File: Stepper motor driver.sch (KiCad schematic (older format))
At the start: 16 parts, among them P1 CONN_01X04, P2 CONN_01X04, Q1 TIP120, Q2 TIP120, Q3 TIP120, Q4 TIP120, U1 74LS175, U2 74LS157

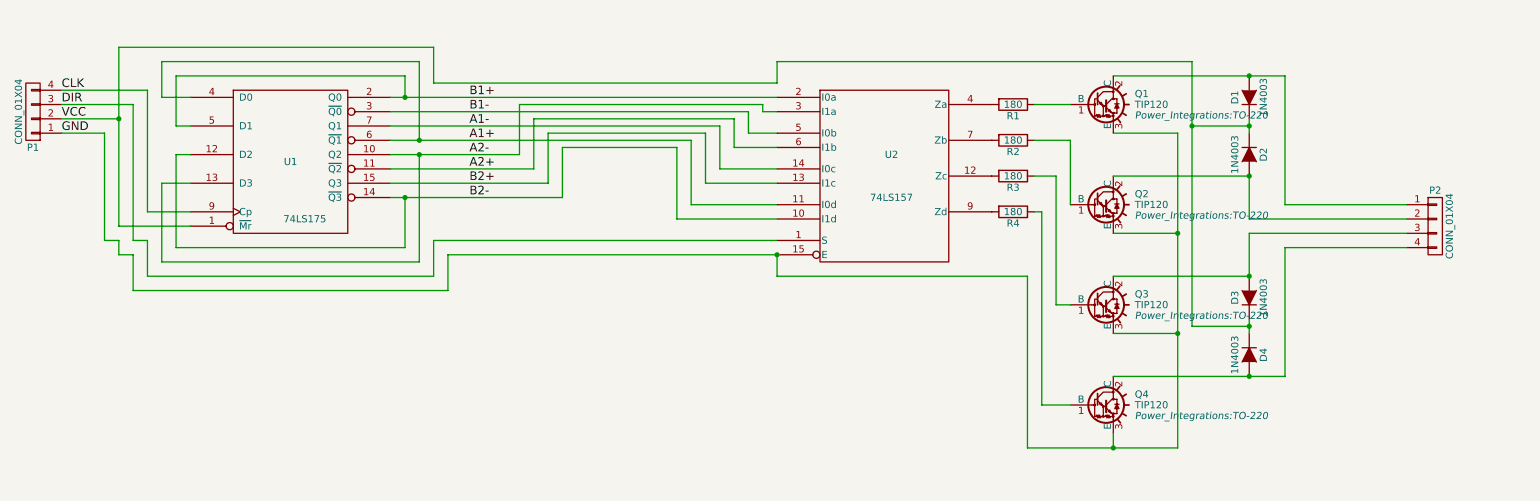
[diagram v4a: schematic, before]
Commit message: Cleaned up schematic and placed PCB components
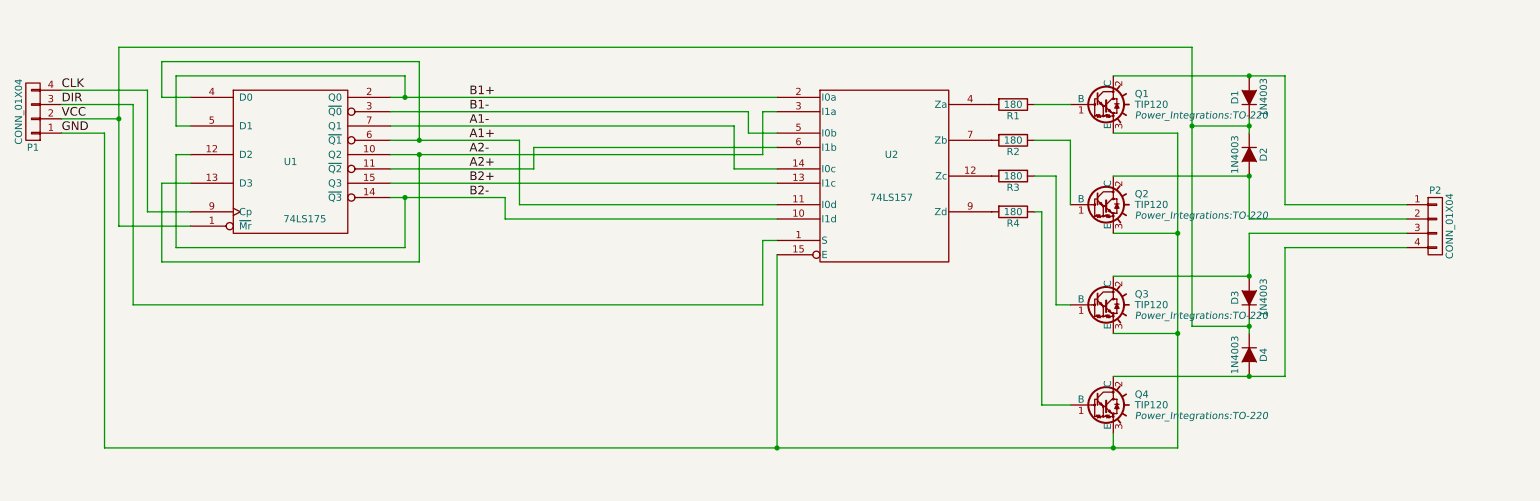
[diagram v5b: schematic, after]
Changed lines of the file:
@@
 	1    0    0    -1
 $EndComp
-Wire Wire Line
-	3150 3750 5250 3750
-Wire Wire Line
-	3150 3450 5850 3450
-Wire Wire Line
-	1650 3300 3250 3300
-Wire Wire Line
-	1650 3300 1650 3650
-Wire Wire Line
-	1650 3650 1750 3650
-Wire Wire Line
-	1550 3200 3350 3200
-Wire Wire Line
-	1550 3200 1550 3450
-Wire Wire Line
-	1550 3450 1750 3450
-Wire Wire Line
-	3150 3850 4050 3850
-Wire Wire Line
-	3150 4150 4350 4150
-Connection ~ 3250 3450
-Connection ~ 3350 3750
-Wire Wire Line
-	3250 3300 3250 3450
-Wire Wire Line
-	3350 3200 3350 3750
-Wire Wire Line
-	3250 4500 3250 4150
-Wire Wire Line
-	1650 4500 3250 4500
-Wire Wire Line
-	1650 4500 1650 3850
-Wire Wire Line
-	1650 3850 1750 3850
-Connection ~ 3250 4150
-Wire Wire Line
-	3350 3850 3350 4600
-Wire Wire Line
-	3350 4600 1550 4600
-Wire Wire Line
-	1550 4600 1550 4050
-Wire Wire Line
-	1550 4050 1750 4050
-Connection ~ 3350 3850
-Wire Wire Line
-	3150 3950 4150 3950
-Wire Wire Line
-	3150 4050 4250 4050
-Wire Wire Line
-	3150 3650 5450 3650
-Wire Wire Line
-	3150 3550 5650 3550
-Wire Wire Line
-	5650 3550 5650 3700
-Wire Wire Line
-	5650 3700 5850 3700
-Wire Wire Line
-	5450 3650 5450 3950
-Wire Wire Line
-	5450 3950 5850 3950
-Wire Wire Line
-	5250 3750 5250 4200
-Wire Wire Line
-	5250 4200 5850 4200
-Wire Wire Line
-	4050 3850 4050 3500
-Wire Wire Line
-	4050 3500 5750 3500
-Wire Wire Line
-	5750 3500 5750 3550
-Wire Wire Line
-	5750 3550 5850 3550
-Wire Wire Line
-	4150 3950 4150 3600
-Wire Wire Line
-	4150 3600 5550 3600
-Wire Wire Line
-	5550 3600 5550 3800
-Wire Wire Line
-	5550 3800 5850 3800
-Wire Wire Line
-	4250 4050 4250 3700
-Wire Wire Line
-	4250 3700 5350 3700
-Wire Wire Line
-	5350 3700 5350 4050
-Wire Wire Line
-	5350 4050 5850 4050
-Wire Wire Line
-	4350 4150 4350 3800
-Wire Wire Line
-	4350 3800 5150 3800
-Wire Wire Line
-	5150 3800 5150 4300
-Wire Wire Line
-	5150 4300 5850 4300
-Wire Wire Line
-	3450 4450 3450 4700
-Wire Wire Line
-	3450 4700 1450 4700
-Wire Wire Line
-	1450 4700 1450 4450
 $Comp
 L R R1
@@
 	0    1    1    0
 $EndComp
-Wire Wire Line
-	7650 3500 7900 3500
-Wire Wire Line
-	7650 3750 7900 3750
-Wire Wire Line
-	7900 3750 7900 4200
-Wire Wire Line
-	7650 4000 7800 4000
-Wire Wire Line
-	7800 4000 7800 4900
-Wire Wire Line
-	7800 4900 7900 4900
-Wire Wire Line
-	7650 4250 7700 4250
-Wire Wire Line
-	7700 4250 7700 5600
-Wire Wire Line
-	7700 5600 7900 5600
 $Comp
 L D D2
@@
 	0    1    1    0
 $EndComp
-Wire Wire Line
-	9150 5000 9150 5100
-Connection ~ 9150 5050
-Wire Wire Line
-	9150 3600 9150 3700
-Connection ~ 8750 3650
-Connection ~ 9150 3650
-Connection ~ 9150 3300
-Connection ~ 9150 4000
-Connection ~ 9150 4700
-Connection ~ 9150 5400
 $Comp
 L TIP120 Q2
@@
 	1    0    0    -1
 $EndComp
-Wire Wire Line
-	5850 4450 3450 4450
-Wire Wire Line
-	3550 4550 5850 4550
 Text Label 850  3500 0    60   ~ 0
 DIR
@@
 	-1   0    0    1
 $EndComp
-Wire Wire Line
-	850  3500 1350 3500
-Wire Wire Line
-	850  3600 1250 3600
 Text Label 850  3600 0    60   ~ 0
 VCC
-Wire Wire Line
-	3550 4800 3550 4550
-Wire Wire Line
-	1350 4800 3550 4800
-Wire Wire Line
-	1350 4800 1350 4550
-Wire Wire Line
-	850  3700 1150 3700
 Text Label 850  3700 0    60   ~ 0
 GND
-Wire Wire Line
-	1750 4250 1450 4250
-Wire Wire Line
-	1450 4250 1450 3400
-Wire Wire Line
-	1450 3400 850  3400
-Wire Wire Line
-	1350 3500 1350 4450
-Wire Wire Line
-	1350 4450 1450 4450
-Wire Wire Line
-	1250 4350 1750 4350
-Wire Wire Line
-	1250 3100 1250 4350
-Wire Wire Line
-	1350 4550 1250 4550
-Wire Wire Line
-	1250 4550 1250 4450
-Wire Wire Line
-	1250 4450 1150 4450
-Wire Wire Line
-	1150 4450 1150 3700
-Wire Wire Line
-	8750 3200 8750 5050
-Wire Wire Line
-	5850 3200 8750 3200
-Wire Wire Line
-	5850 3200 5850 3350
-Wire Wire Line
-	5850 3350 3450 3350
-Wire Wire Line
-	3450 3350 3450 3100
-Wire Wire Line
-	3450 3100 1250 3100
-Connection ~ 1250 3600
-Wire Wire Line
-	9150 3650 8750 3650
-Wire Wire Line
-	8750 5050 9150 5050
-Wire Wire Line
-	8650 5900 8650 3700
-Wire Wire Line
-	7600 5900 8650 5900
-Wire Wire Line
-	8200 5800 8200 5900
-Connection ~ 8200 5900
-Wire Wire Line
-	8200 5100 8650 5100
-Connection ~ 8650 5100
-Wire Wire Line
-	8650 3700 8200 3700
-Wire Wire Line
-	8200 4400 8650 4400
-Connection ~ 8650 4400
-Wire Wire Line
-	7600 5900 7600 4700
-Wire Wire Line
-	7600 4700 5850 4700
-Wire Wire Line
-	5850 4700 5850 4550
-Connection ~ 5850 4550
 $Comp
 L CONN_01X04 P2
@@
 $EndComp
 Wire Wire Line
+	3150 3450 5850 3450
+Wire Wire Line
+	1650 3300 3250 3300
+Wire Wire Line
+	1650 3300 1650 3650
+Wire Wire Line
+	1650 3650 1750 3650
+Wire Wire Line
+	1550 3200 3350 3200
+Wire Wire Line
+	1550 3200 1550 3450
+Wire Wire Line
+	1550 3450 1750 3450
+Wire Wire Line
+	5750 3850 3150 3850
+Connection ~ 3250 3450
+Connection ~ 3350 3750
+Wire Wire Line
+	3250 3300 3250 3450
+Wire Wire Line
+	3350 3200 3350 3750
+Wire Wire Line
+	3250 4500 3250 4150
+Wire Wire Line
+	1650 4500 3250 4500
+Wire Wire Line
+	1650 4500 1650 3850
+Wire Wire Line
+	1650 3850 1750 3850
+Connection ~ 3250 4150
+Wire Wire Line
+	3350 3850 3350 4600
+Wire Wire Line
+	3350 4600 1550 4600
+Wire Wire Line
+	1550 4600 1550 4050
+Wire Wire Line
+	1550 4050 1750 4050
+Connection ~ 3350 3850
+Wire Wire Line
+	3150 4050 5850 4050
+Wire Wire Line
+	3150 3650 5550 3650
+Wire Wire Line
+	3150 3550 5650 3550
+Wire Wire Line
+	5650 3550 5650 3700
+Wire Wire Line
+	5650 3700 5850 3700
+Wire Wire Line
+	4050 4200 5850 4200
+Wire Wire Line
+	5750 3550 5850 3550
+Wire Wire Line
+	3950 4300 5850 4300
+Wire Wire Line
+	7650 3500 7900 3500
+Wire Wire Line
+	7650 3750 7900 3750
+Wire Wire Line
+	7900 3750 7900 4200
+Wire Wire Line
+	7650 4000 7800 4000
+Wire Wire Line
+	7800 4000 7800 4900
+Wire Wire Line
+	7800 4900 7900 4900
+Wire Wire Line
+	7650 4250 7700 4250
+Wire Wire Line
+	7700 4250 7700 5600
+Wire Wire Line
+	7700 5600 7900 5600
+Wire Wire Line
+	9150 5000 9150 5100
+Connection ~ 9150 5050
+Wire Wire Line
+	9150 3600 9150 3700
+Connection ~ 8750 3650
+Connection ~ 9150 3650
+Connection ~ 9150 3300
+Connection ~ 9150 4000
+Connection ~ 9150 4700
+Connection ~ 9150 5400
+Wire Wire Line
+	850  3500 1350 3500
+Wire Wire Line
+	850  3600 1250 3600
+Wire Wire Line
+	850  3700 1150 3700
+Wire Wire Line
+	1750 4250 1450 4250
+Wire Wire Line
+	1450 4250 1450 3400
+Wire Wire Line
+	1450 3400 850  3400
+Wire Wire Line
+	1350 3500 1350 4900
+Wire Wire Line
+	1250 4350 1750 4350
+Wire Wire Line
+	1250 3100 1250 4350
+Wire Wire Line
+	8750 3100 8750 5050
+Wire Wire Line
+	1250 3100 8750 3100
+Connection ~ 1250 3600
+Wire Wire Line
+	9150 3650 8750 3650
+Wire Wire Line
+	8750 5050 9150 5050
+Wire Wire Line
+	8650 5900 8650 3700
+Wire Wire Line
+	1150 5900 8650 5900
+Wire Wire Line
+	8200 5800 8200 5900
+Connection ~ 8200 5900
+Wire Wire Line
+	8200 5100 8650 5100
+Connection ~ 8650 5100
+Wire Wire Line
+	8650 3700 8200 3700
+Wire Wire Line
+	8200 4400 8650 4400
+Connection ~ 8650 4400
+Wire Wire Line
+	5850 4550 5850 5900
+Wire Wire Line
 	8200 3300 9400 3300
 Wire Wire Line
@@
 Wire Wire Line
 	9150 4700 8200 4700
+Wire Wire Line
+	1150 3700 1150 5900
+Connection ~ 5850 5900
+Wire Wire Line
+	1350 4900 5750 4900
+Wire Wire Line
+	5750 4900 5750 4450
+Wire Wire Line
+	5750 4450 5850 4450
+Wire Wire Line
+	3150 4150 3950 4150
+Wire Wire Line
+	3150 3750 4050 3750
+Wire Wire Line
+	3950 4150 3950 4300
+Wire Wire Line
+	4050 3750 4050 4200
+Wire Wire Line
+	5750 3850 5750 3550
+Wire Wire Line
+	5550 3650 5550 3950
+Wire Wire Line
+	5550 3950 5850 3950
+Wire Wire Line
+	4150 3800 5850 3800
+Wire Wire Line
+	4150 3950 4150 3800
+Wire Wire Line
+	3150 3950 4150 3950
 $EndSCHEMATC

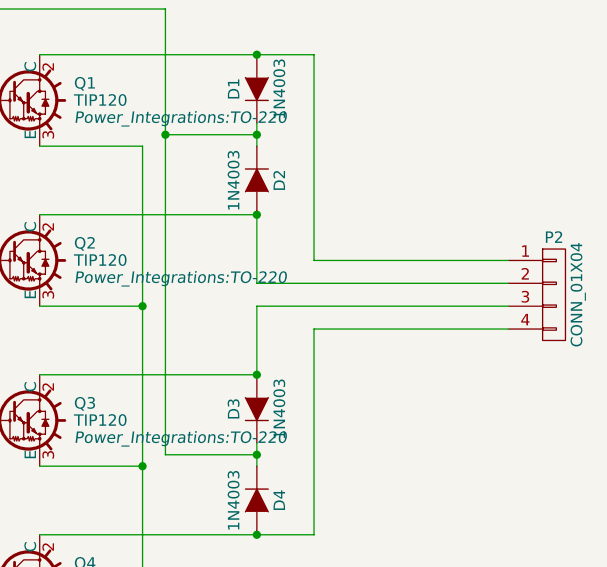
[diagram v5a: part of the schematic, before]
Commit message: Small schematic change, fine component placement, silkscreen
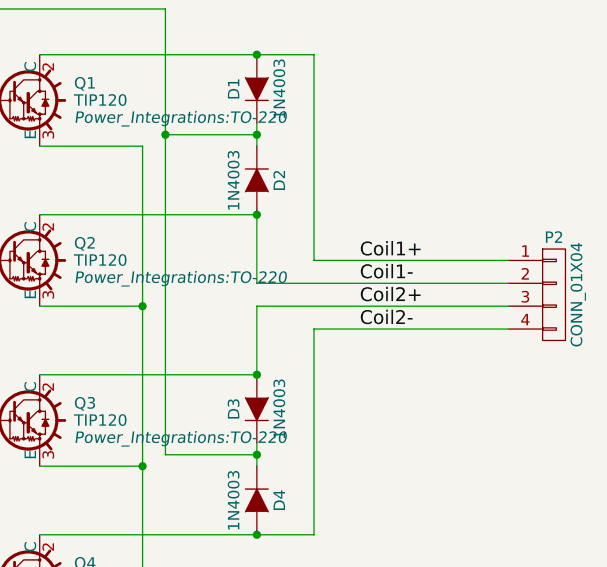
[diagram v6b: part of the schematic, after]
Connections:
- net Coil1+: now reaches D1.2 (A), P2.1 (P1), Q1.2 (C)
- net Coil1-: now reaches D2.2 (A), P2.2 (P2), Q2.2 (C)
- net Coil2+: now reaches D3.2 (A), P2.3 (P3), Q3.2 (C)
- net Coil2-: now reaches D4.2 (A), P2.4 (P4), Q4.2 (C)
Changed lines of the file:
@@
 Wire Wire Line
 	3150 3950 4150 3950
+Text Label 9600 4200 0    60   ~ 0
+Coil1+
+Text Label 9600 4300 0    60   ~ 0
+Coil1-
+Text Label 9600 4400 0    60   ~ 0
+Coil2+
+Text Label 9600 4500 0    60   ~ 0
+Coil2-
 $EndSCHEMATC

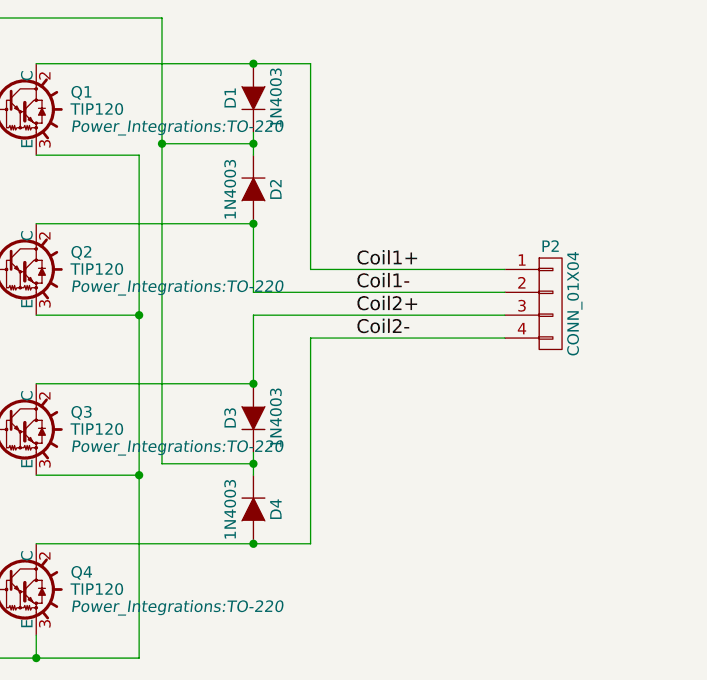
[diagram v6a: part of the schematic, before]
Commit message: Added VCC to output, initial board routing
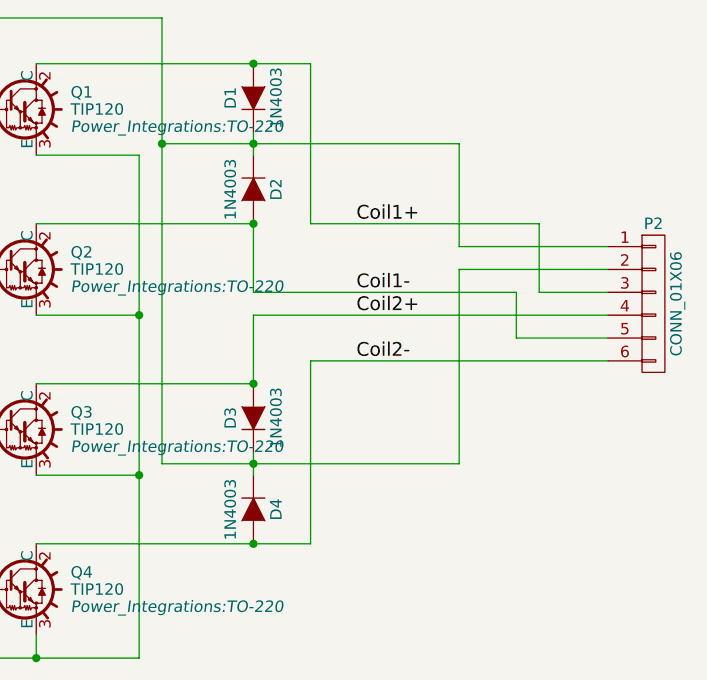
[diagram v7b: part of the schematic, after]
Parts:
- removed P2: CONN_01X04, Connect:Grove_1x04, symbol CONN_01X04
- added P2: CONN_01X06, Connectors_Molex:Molex_KK-6410-06_06x2.54mm_Straight, symbol CONN_01X06
- P1: footprint Connect:Grove_1x04 -> Connectors_Molex:Molex_KK-6410-04_04x2.54mm_Straight
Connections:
- net Coil1+: now also P2.3 (P3)
- net Coil1-: now also P2.5 (P5)
- net Coil2+: now also P2.4 (P4)
- net Coil2-: now also P2.6 (P6)
- net VCC: now also P2.1 (P1), P2.2 (P2)
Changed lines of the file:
@@
 F 0 "P1" H 650 3800 50  0000 C CNN
 F 1 "CONN_01X04" V 750 3550 50  0000 C CNN
-F 2 "Connect:Grove_1x04" H 650 3550 50  0001 C CNN
+F 2 "Connectors_Molex:Molex_KK-6410-04_04x2.54mm_Straight" H 650 3550 50  0001 C CNN
 F 3 "" H 650 3550 50  0000 C CNN
 	1    650  3550
@@
 Text Label 850  3700 0    60   ~ 0
 GND
+Text Label 9600 4000 0    60   ~ 0
+Coil1+
+Text Label 9600 4300 0    60   ~ 0
+Coil1-
+Text Label 9600 4400 0    60   ~ 0
+Coil2+
+Text Label 9600 4600 0    60   ~ 0
+Coil2-
 $Comp
-L CONN_01X04 P2
-U 1 1 58AD964B
-P 10450 4350
-F 0 "P2" H 10450 4600 50  0000 C CNN
-F 1 "CONN_01X04" V 10550 4350 50  0000 C CNN
-F 2 "Connect:Grove_1x04" H 10450 4350 50  0001 C CNN
-F 3 "" H 10450 4350 50  0000 C CNN
-	1    10450 4350
+L CONN_01X06 P2
+U 1 1 58B0F217
+P 10900 4350
+F 0 "P2" H 10900 4700 50  0000 C CNN
+F 1 "CONN_01X06" V 11000 4350 50  0000 C CNN
+F 2 "Connectors_Molex:Molex_KK-6410-06_06x2.54mm_Straight" H 10900 4350 50  0001 C CNN
+F 3 "" H 10900 4350 50  0000 C CNN
+	1    10900 4350
 	1    0    0    -1
 $EndComp
@@
 Connection ~ 1250 3600
 Wire Wire Line
-	9150 3650 8750 3650
-Wire Wire Line
-	8750 5050 9150 5050
+	8750 3650 10050 3650
+Wire Wire Line
+	8750 5050 10050 5050
 Wire Wire Line
 	8650 5900 8650 3700
@@
 	8200 3300 9400 3300
 Wire Wire Line
-	9400 3300 9400 4200
-Wire Wire Line
-	9400 4200 10250 4200
-Wire Wire Line
 	8200 4000 9150 4000
 Wire Wire Line
 	9150 4000 9150 4300
 Wire Wire Line
-	9150 4300 10250 4300
+	9150 4300 10300 4300
 Wire Wire Line
 	8200 5400 9400 5400
 Wire Wire Line
-	9400 5400 9400 4500
-Wire Wire Line
-	9400 4500 10250 4500
-Wire Wire Line
-	10250 4400 9150 4400
+	9150 4400 10700 4400
 Wire Wire Line
 	9150 4400 9150 4700
@@
 Wire Wire Line
 	3150 3950 4150 3950
-Text Label 9600 4200 0    60   ~ 0
-Coil1+
-Text Label 9600 4300 0    60   ~ 0
-Coil1-
-Text Label 9600 4400 0    60   ~ 0
-Coil2+
-Text Label 9600 4500 0    60   ~ 0
-Coil2-
+Wire Wire Line
+	9400 5400 9400 4600
+Wire Wire Line
+	9400 4600 10700 4600
+Wire Wire Line
+	10050 5050 10050 4200
+Wire Wire Line
+	10400 4300 10700 4300
+Wire Wire Line
+	10050 3650 10050 4100
+Wire Wire Line
+	10050 4100 10700 4100
+Wire Wire Line
+	10050 4200 10700 4200
+Wire Wire Line
+	9400 3300 9400 4000
+Wire Wire Line
+	9400 4000 10400 4000
+Wire Wire Line
+	10400 4000 10400 4300
+Wire Wire Line
+	10300 4300 10300 4500
+Wire Wire Line
+	10300 4500 10700 4500
 $EndSCHEMATC

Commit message: Continued routing progress
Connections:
- net CLK: now also P1.2 (P2); no longer P1.4 (P4)
- net GND: now also P1.4 (P4); no longer P1.1 (P1)
- net VCC: now also P1.1 (P1); no longer P1.2 (P2)
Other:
- moved on the sheet: D1, D2, D3, D4, P1, P2, Q1, Q2, Q3, Q4, R1, R2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
